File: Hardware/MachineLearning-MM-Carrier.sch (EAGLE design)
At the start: 59 parts, among them J11 microSD, J2 JTAG, J3 QWIIC_RIGHT_ANGLE, J9 MICROMOD-2222-C, U1 BME280, U2 VEML6075, U5 AP7361C-33FGE

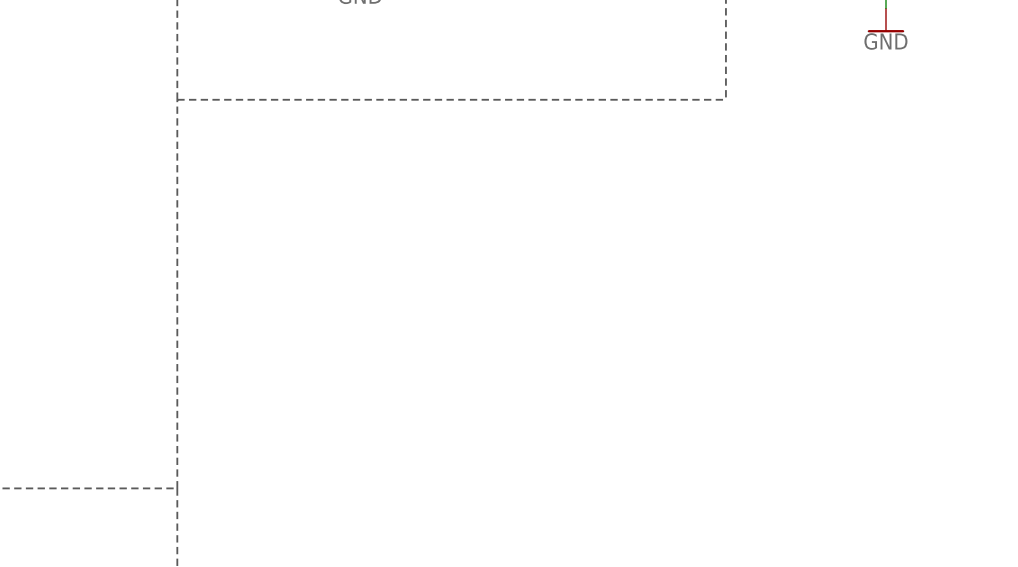
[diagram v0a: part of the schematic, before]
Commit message: Added connector for soil moisture sensor
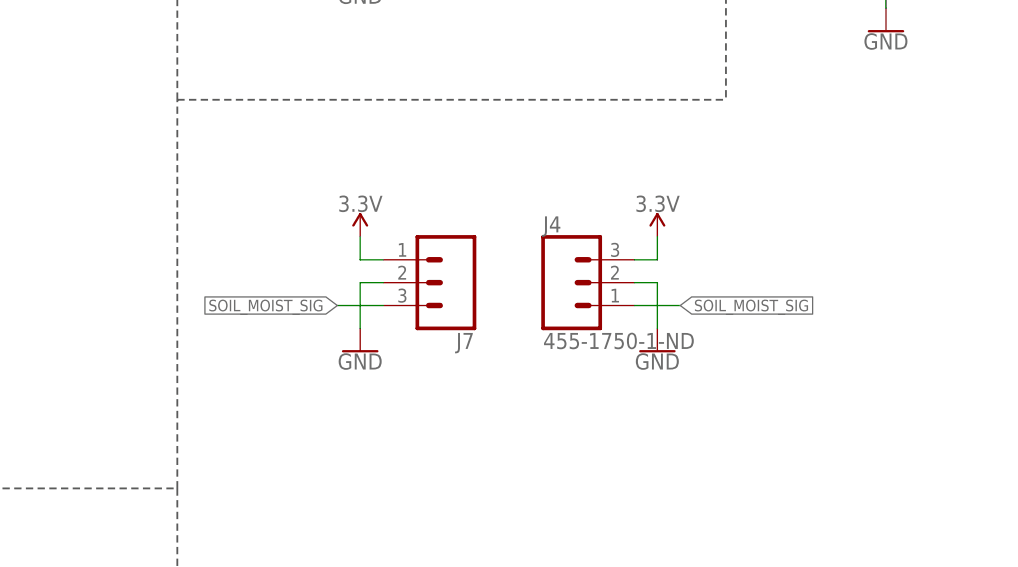
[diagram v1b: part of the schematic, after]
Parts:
- added J4: 455-1750-1-ND, SparkFun-Connectors:CONN_03
- added J7: (no value), SparkFun-Connectors:CONN_03SCREW
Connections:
- new net SOIL_MOIST_SIG: J4.1, J7.3
- net 3.3V: now also J4.3, J7.1
- net GND: now also J4.2, J7.2
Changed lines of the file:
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@@
 <part name="GND27" library="SparkFun-PowerSymbols" deviceset="GND" device=""/>
 <part name="SUPPLY14" library="SparkFun-PowerSymbols" deviceset="3.3V" device=""/>
+<part name="J4" library="SparkFun-Connectors" deviceset="CONN_03" device="" value="455-1750-1-ND"/>
+<part name="J7" library="SparkFun-Connectors" deviceset="CONN_03" device="SCREW"/>
+<part name="GND28" library="SparkFun-PowerSymbols" deviceset="GND" device=""/>
+<part name="GND29" library="SparkFun-PowerSymbols" deviceset="GND" device=""/>
+<part name="SUPPLY15" library="SparkFun-PowerSymbols" deviceset="3.3V" device=""/>
+<part name="SUPPLY21" library="SparkFun-PowerSymbols" deviceset="3.3V" device=""/>
 </parts>
 <sheets>
@@
 <attribute name="VALUE" x="381" y="254.254" size="1.778" layer="96" align="bottom-center"/>
 </instance>
+<instance part="J4" gate="J$1" x="210.82" y="195.58" smashed="yes">
+<attribute name="VALUE" x="208.28" y="188.214" size="1.778" layer="96" font="vector"/>
+<attribute name="NAME" x="208.28" y="201.168" size="1.778" layer="95" font="vector"/>
+</instance>
+<instance part="J7" gate="J$1" x="198.12" y="195.58" smashed="yes" rot="R180">
+<attribute name="VALUE" x="200.66" y="202.946" size="1.778" layer="96" font="vector" rot="R180"/>
+<attribute name="NAME" x="200.66" y="189.992" size="1.778" layer="95" font="vector" rot="R180"/>
+</instance>
+<instance part="GND28" gate="1" x="220.98" y="187.96" smashed="yes">
+<attribute name="VALUE" x="220.98" y="187.706" size="1.778" layer="96" align="top-center"/>
+</instance>
+<instance part="GND29" gate="1" x="187.96" y="187.96" smashed="yes">
+<attribute name="VALUE" x="187.96" y="187.706" size="1.778" layer="96" align="top-center"/>
+</instance>
+<instance part="SUPPLY15" gate="G$1" x="187.96" y="200.66" smashed="yes">
+<attribute name="VALUE" x="187.96" y="203.454" size="1.778" layer="96" align="bottom-center"/>
+</instance>
+<instance part="SUPPLY21" gate="G$1" x="220.98" y="200.66" smashed="yes">
+<attribute name="VALUE" x="220.98" y="203.454" size="1.778" layer="96" align="bottom-center"/>
+</instance>
 </instances>
 <busses>
@@
 <wire x1="381" y1="243.84" x2="381" y2="241.3" width="0.1524" layer="91"/>
 </segment>
+<segment>
+<pinref part="J7" gate="J$1" pin="2"/>
+<wire x1="190.5" y1="195.58" x2="187.96" y2="195.58" width="0.1524" layer="91"/>
+<pinref part="GND29" gate="1" pin="GND"/>
+<wire x1="187.96" y1="195.58" x2="187.96" y2="190.5" width="0.1524" layer="91"/>
+</segment>
+<segment>
+<pinref part="J4" gate="J$1" pin="2"/>
+<wire x1="218.44" y1="195.58" x2="220.98" y2="195.58" width="0.1524" layer="91"/>
+<pinref part="GND28" gate="1" pin="GND"/>
+<wire x1="220.98" y1="195.58" x2="220.98" y2="190.5" width="0.1524" layer="91"/>
+</segment>
 </net>
 <net name="3.3V" class="0">
@@
 <pinref part="SUPPLY14" gate="G$1" pin="3.3V"/>
 <wire x1="381" y1="248.92" x2="381" y2="251.46" width="0.1524" layer="91"/>
+</segment>
+<segment>
+<pinref part="J7" gate="J$1" pin="1"/>
+<wire x1="190.5" y1="198.12" x2="187.96" y2="198.12" width="0.1524" layer="91"/>
+<pinref part="SUPPLY15" gate="G$1" pin="3.3V"/>
+<wire x1="187.96" y1="198.12" x2="187.96" y2="200.66" width="0.1524" layer="91"/>
+</segment>
+<segment>
+<pinref part="J4" gate="J$1" pin="3"/>
+<wire x1="218.44" y1="198.12" x2="220.98" y2="198.12" width="0.1524" layer="91"/>
+<pinref part="SUPPLY21" gate="G$1" pin="3.3V"/>
+<wire x1="220.98" y1="198.12" x2="220.98" y2="200.66" width="0.1524" layer="91"/>
 </segment>
 </net>
@@
 </segment>
 </net>
+<net name="SOIL_MOIST_SIG" class="0">
+<segment>
+<pinref part="J7" gate="J$1" pin="3"/>
+<wire x1="190.5" y1="193.04" x2="185.42" y2="193.04" width="0.1524" layer="91"/>
+<label x="185.42" y="193.04" size="1.27" layer="95" rot="R180" xref="yes"/>
+</segment>
+<segment>
+<pinref part="J4" gate="J$1" pin="1"/>
+<wire x1="218.44" y1="193.04" x2="223.52" y2="193.04" width="0.1524" layer="91"/>
+<label x="223.52" y="193.04" size="1.27" layer="95" xref="yes"/>
+</segment>
+</net>

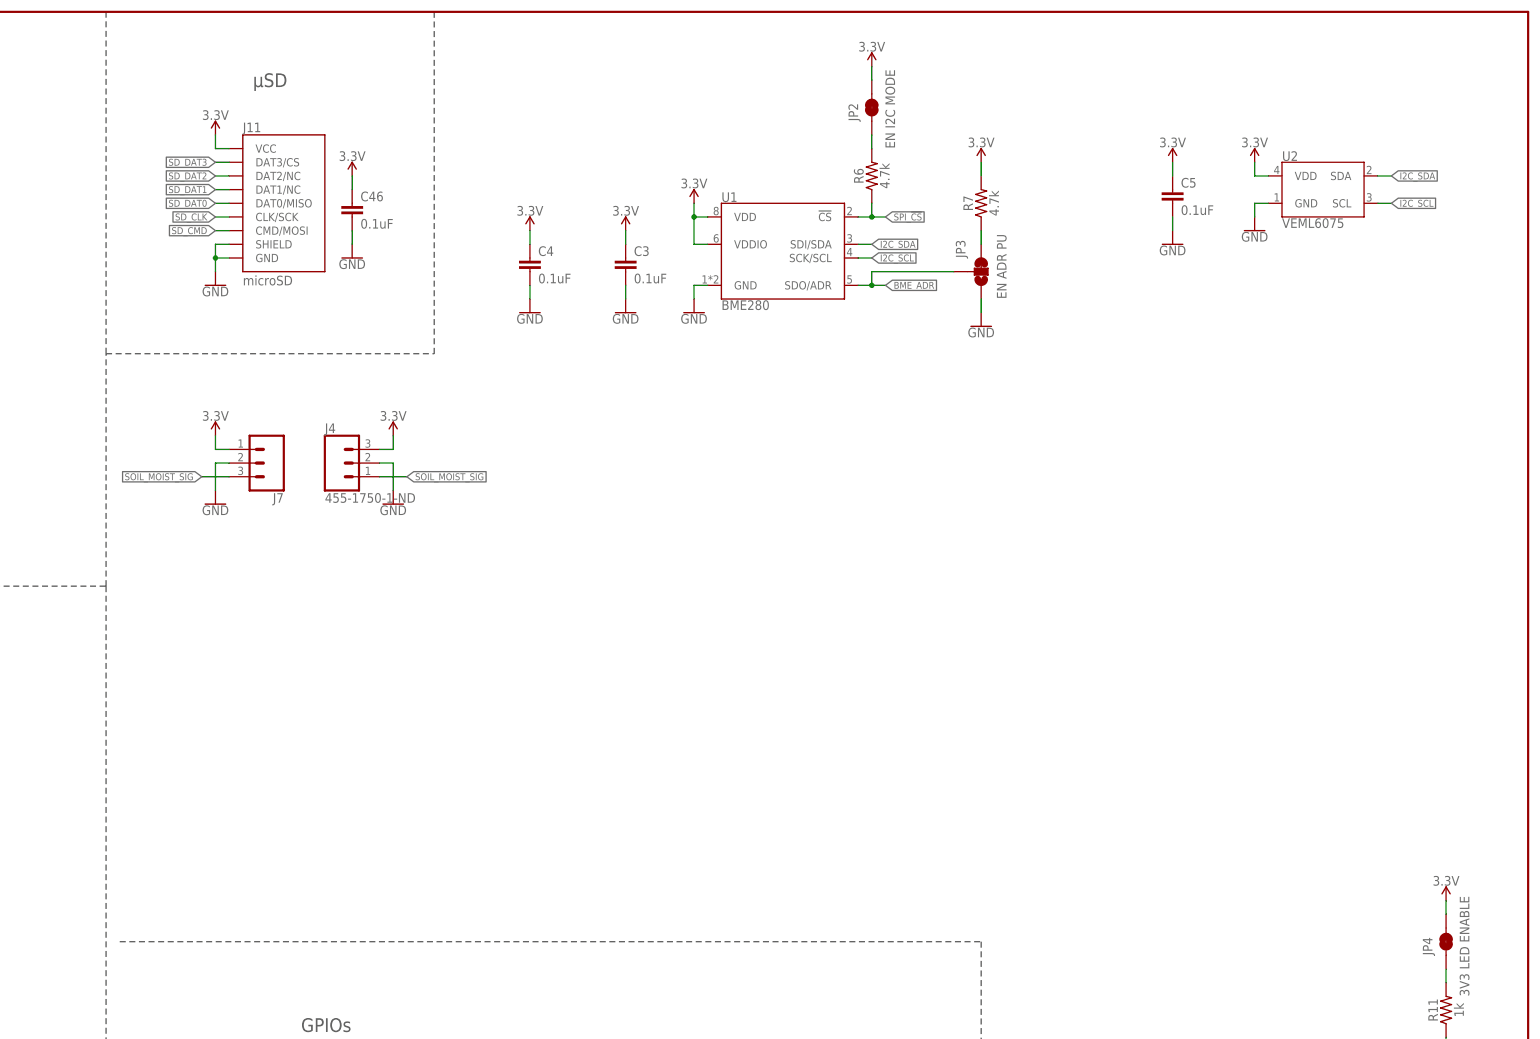
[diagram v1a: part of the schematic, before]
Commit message: Added RJ11 connectors for weather station add-on
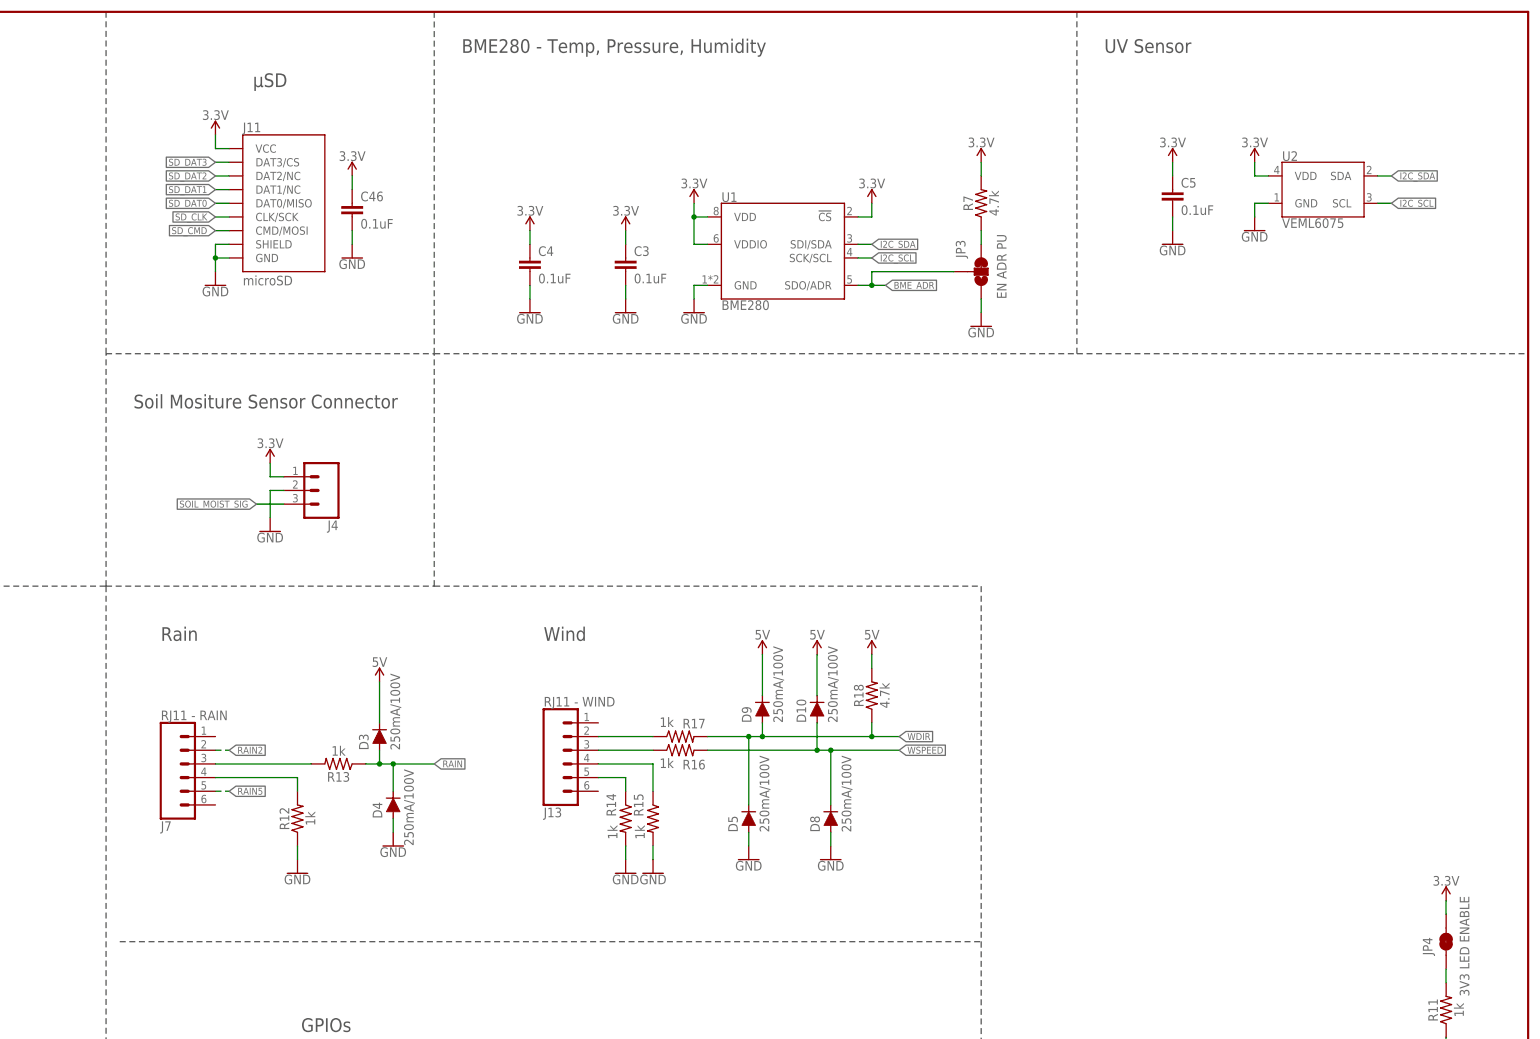
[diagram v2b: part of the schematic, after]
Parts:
- removed JP2: EN I2C MODE, SparkFun-Jumpers:JUMPER-SMT_2_NC_TRACE_SILK
- removed R6: 4.7k, SparkFun-Resistors:4.7KOHM-0603-1/10W-1%
- added D10, D3, D4, D5, D8, D9: 250mA/100V, SparkFun-DiscreteSemi:DIODE-BAS16J
- added J13: RJ11 - WIND, SparkFun-Connectors:RJ11-6
- added R12, R13, R14, R15, R16, R17: 1k, SparkFun-Resistors:1KOHM-0603-1/10W-1%
- added R18: 4.7k, SparkFun-Resistors:4.7KOHM-0603-1/10W-1%
- J4: value 455-1750-1-ND -> (none); device SparkFun-Connectors:CONN_03 -> SparkFun-Connectors:CONN_03LATCH
- J7: value (none) -> RJ11 - RAIN; device SparkFun-Connectors:CONN_03SCREW -> SparkFun-Connectors:RJ11-6
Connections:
- removed net N$5: JP2.1, R6.2
- new net 5V: D10.C, D3.C, D9.C, R18.2
- new net N$12: J13.5, R14.1
- new net N$13: J13.4, R15.1
- new net N$17: J13.3, R16.1
- new net N$18: J13.2, R17.1
- new net N$7: J7.4, R12.2
- new net N$9: J7.3, R13.2
- new net RAIN: D3.A, D4.C, R13.1
- new net RAIN2: J7.2
- new net RAIN5: J7.5
- new net WDIR: D5.C, D9.A, R17.2, R18.1
- new net WSPEED: D10.A, D8.C, R16.2
- net 3.3V: now also J4.1, U1.!CS; no longer J4.3, J7.1, JP2.2
- net GND: now also D4.A, D5.A, D8.A, R12.1, R14.2, R15.2; no longer J7.2
- net SOIL_MOIST_SIG: now also J4.3; no longer J4.1, J7.3
- net SPI_!CS!: no longer R6.1, U1.!CS
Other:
- note added: "BME280 - Temp, Pressure, Humidity"
- note added: "Rain"
- note added: "Soil Mositure Sensor Connector"
- note added: "UV Sensor"
- note added: "Wind"
- moved on the sheet: J4

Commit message: Added lightning detector block
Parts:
- added C6: 1.0uF, SparkFun-Capacitors:1.0UF-0603-16V-10%
- added C7: 10uF, SparkFun-Capacitors:10UF-0603-6.3V-20%
- added C8: 1nF, SparkFun-Capacitors:1.0NF/1000PF-0603-50V-10%
- added D11: Yellow, SparkFun-LED:LED-YELLOW0603
- added JP2: VIN LED ENABLE, SparkFun-Jumpers:JUMPER-SMT_2_NC_TRACE_SILK
- added L1: 100uH, SparkFun-Coils:MA5532-AE
- added R19, R6: 10k, SparkFun-Resistors:10KOHM-0603-1/10W-1%
- added R20: 1k, SparkFun-Resistors:1KOHM-0603-1/10W-1%
- added U3: AS3935, SparkFun-Sensors:AS3935QFN
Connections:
- new net INP: C8.1, L1.1, R6.2, U3.INP
- new net LIGHTNING_INT: U3.IRQ
- new net N$15: C7.1, U3.AC_GND
- new net N$16: D11.A, R20.1
- new net N$5: JP2.1, R20.2
- net 3.3V: now also C6.1, R19.2, U3.VDD, U3.VREG
- net GND: now also C6.2, C7.2, C8.2, D11.C, L1.2, R6.1, U3.EN_VREG, U3.GND, U3.GND_PAD, U3.INN, U3.SI
- net SPI_!CS!: now also R19.1, U3.!CS
- net SPI_CLK: now also U3.SCL/I2CL
- net SPI_MISO: now also U3.MISO
- net SPI_MOSI: now also U3.MOSI/I2CD
- net VIN: now also JP2.2
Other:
- note added: "LED's"
- note added: "Lightning Detector"
- moved on the sheet: BT1, BYP, C1, C13, C2, C3, C4, D1, D2, D6, D7, F2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
